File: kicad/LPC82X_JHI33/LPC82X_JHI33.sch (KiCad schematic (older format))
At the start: 20 parts, among them U1 LPC824M201JHI33

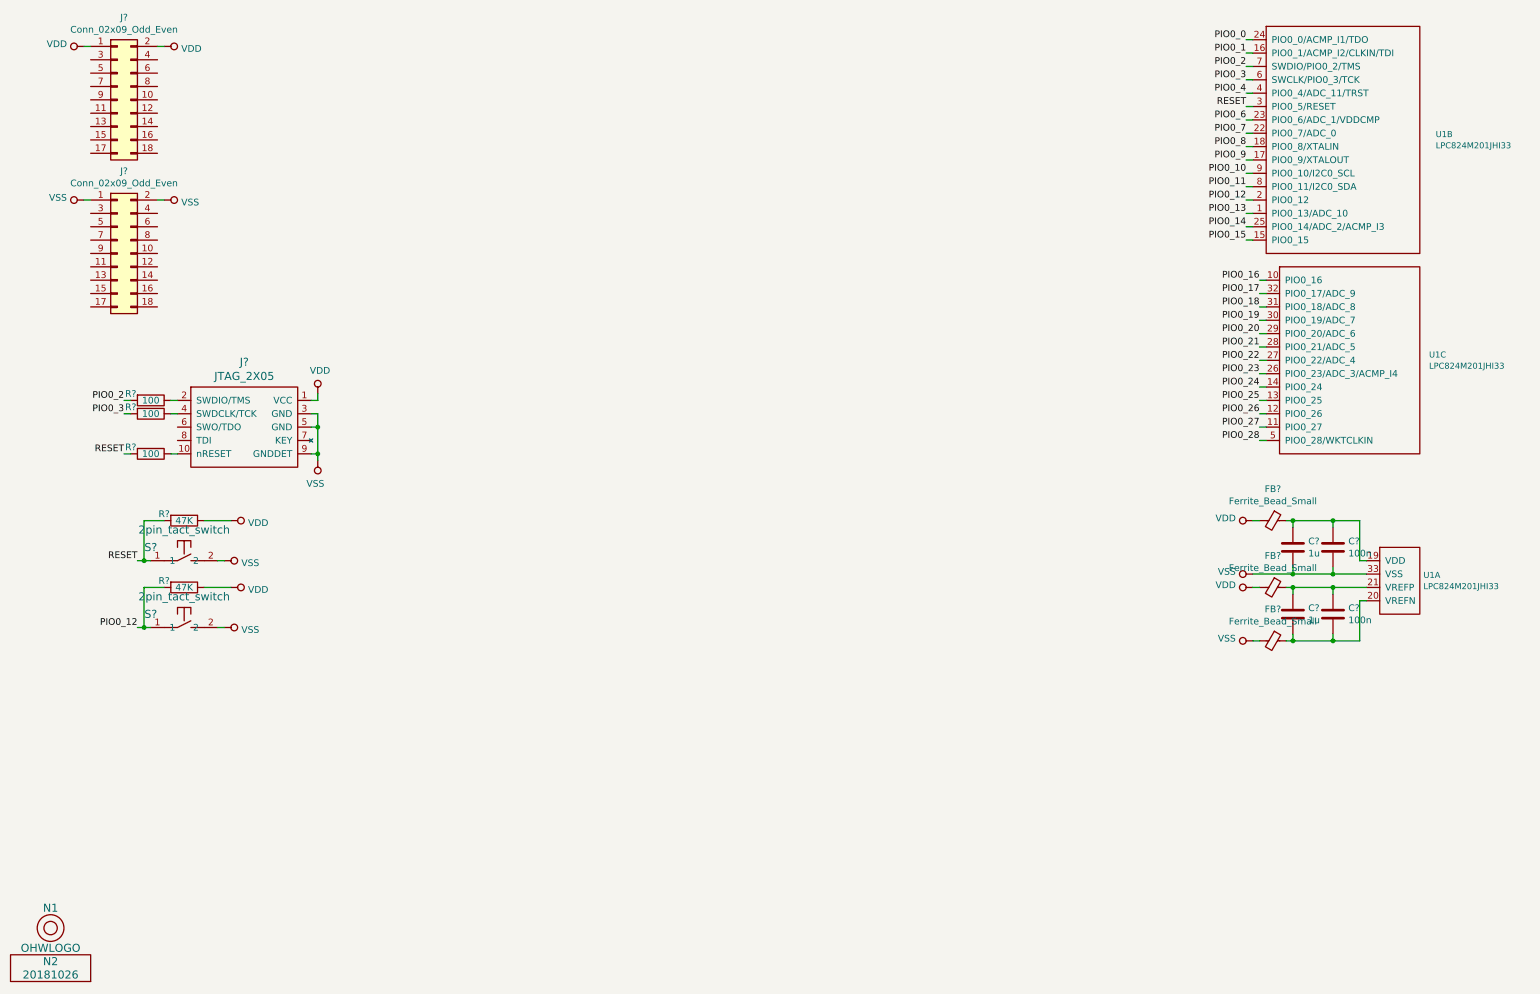
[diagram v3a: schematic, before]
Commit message: updated with solder jumper schematic symbols added some jumpers to the QFN33 breakout
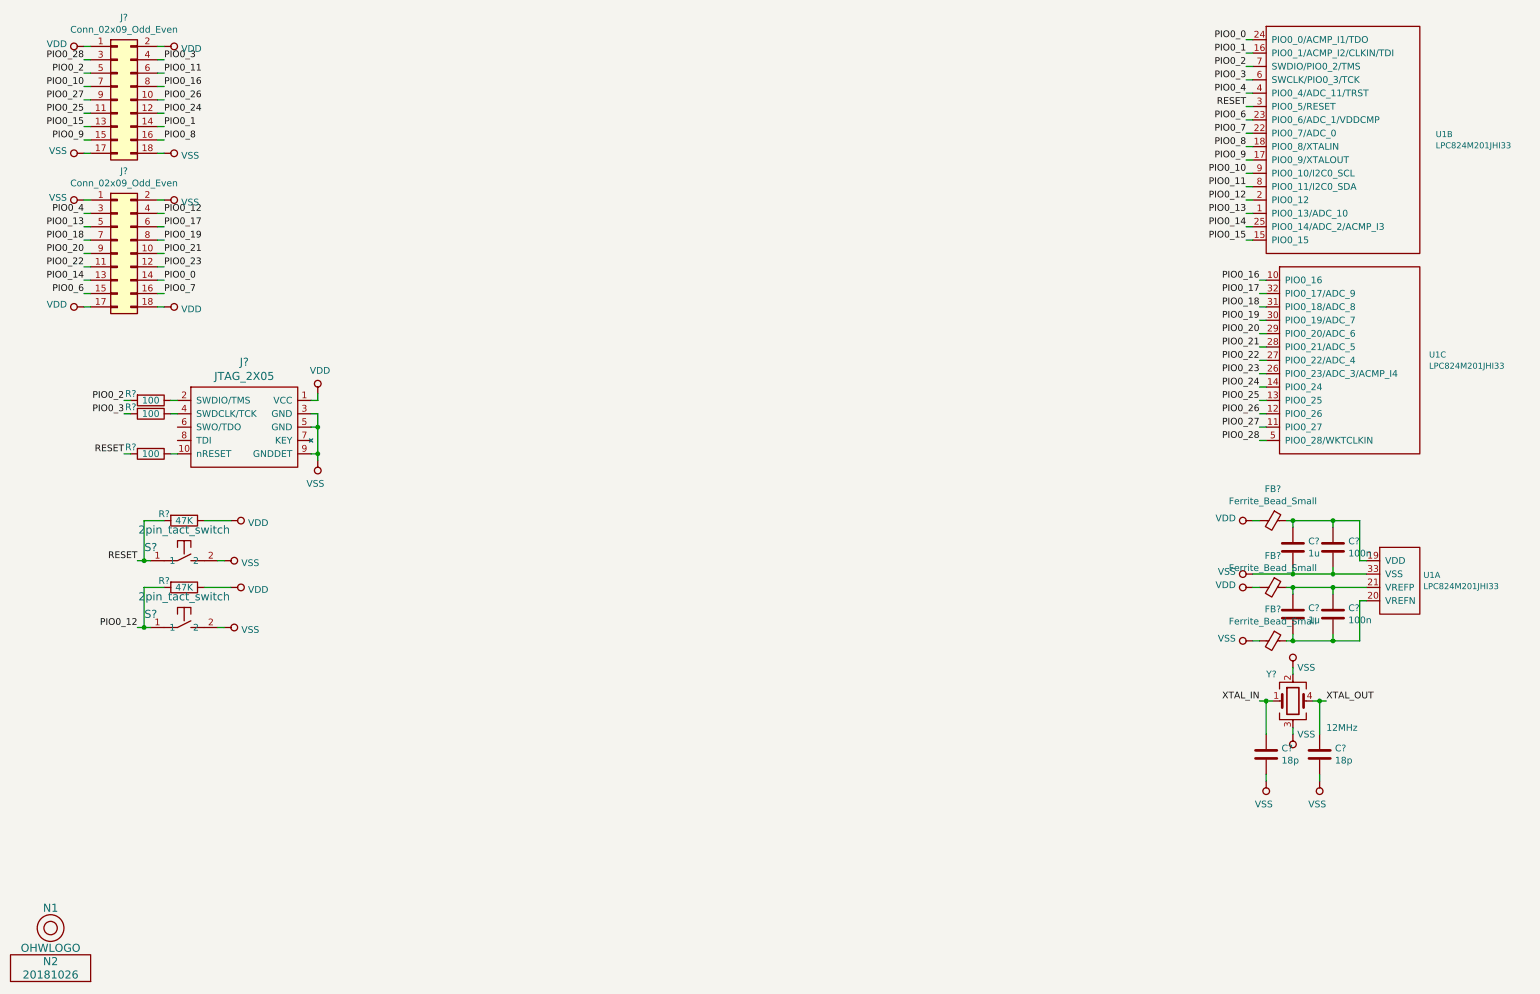
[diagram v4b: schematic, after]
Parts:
- added C? (x2): 18p, SquantorRcl:C_0402, symbol Device:C
- added Y?: 12MHz, symbol Device:Crystal_GND23
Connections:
- net PIO0_0: now also J?.14 (Pin_14)
- net PIO0_1: now also J?.14 (Pin_14)
- net PIO0_10: now also J?.7 (Pin_7)
- net PIO0_11: now also J?.6 (Pin_6)
- net PIO0_12: now also J?.4 (Pin_4)
- net PIO0_13: now also J?.5 (Pin_5)
- net PIO0_14: now also J?.13 (Pin_13)
- net PIO0_15: now also J?.13 (Pin_13)
- net PIO0_16: now also J?.8 (Pin_8)
- net PIO0_17: now also J?.6 (Pin_6)
- net PIO0_18: now also J?.7 (Pin_7)
- net PIO0_19: now also J?.8 (Pin_8)
- net PIO0_2: now also J?.5 (Pin_5)
- net PIO0_20: now also J?.9 (Pin_9)
- net PIO0_21: now also J?.10 (Pin_10)
- net PIO0_22: now also J?.11 (Pin_11)
- net PIO0_23: now also J?.12 (Pin_12)
- net PIO0_24: now also J?.12 (Pin_12)
- net PIO0_25: now also J?.11 (Pin_11)
- net PIO0_26: now also J?.10 (Pin_10)
- net PIO0_27: now also J?.9 (Pin_9)
- net PIO0_28: now also J?.3 (Pin_3)
- net PIO0_3: now also J?.4 (Pin_4)
- net PIO0_4: now also J?.3 (Pin_3)
- net PIO0_6: now also J?.15 (Pin_15)
- net PIO0_7: now also J?.16 (Pin_16)
- net PIO0_8: now also J?.16 (Pin_16)
- net PIO0_9: now also J?.15 (Pin_15)
- net VDD: now also J?.17 (Pin_17), J?.18 (Pin_18)
- net VSS: now also J?.17 (Pin_17), J?.18 (Pin_18), C?.2, C?.2, Y?.2, Y?.3
- new net XTAL_IN: C?.1, Y?.1
- new net XTAL_OUT: C?.1, Y?.4

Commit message: added cystal
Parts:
- added SJ? (x2): SolderJumper_3way_1conn, symbol SquantorSpecial:SolderJumper_3way_1conn
- Y?: footprint (none) -> SquantorCrystal:Crystal_3225_4
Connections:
- net PIO0_8: now also SJ?.1; no longer U1.18 (PIO0_8/XTALIN)
- net PIO0_9: now also SJ?.1; no longer U1.17 (PIO0_9/XTALOUT)
- net XTAL_IN renamed XTALIN
- net XTALIN: now also SJ?.3
- net XTAL_OUT renamed XTALOUT
- net XTALOUT: now also SJ?.3
- new net PIO0_8-XTALIN: SJ?.2, U1.18 (PIO0_8/XTALIN)
- new net PIO0_9-XTALOUT: SJ?.2, U1.17 (PIO0_9/XTALOUT)
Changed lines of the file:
@@
 PIO0_7
 Text Label 9800 1500 2    50   ~ 0
-PIO0_8
+PIO0_8-XTALIN
 Text Label 9800 1600 2    50   ~ 0
-PIO0_9
+PIO0_9-XTALOUT
 Text Label 9800 1700 2    50   ~ 0
 PIO0_10
@@
 F 0 "Y?" H 9950 5850 50  0000 L CNN
 F 1 "12MHz" H 10400 5450 50  0000 L CNN
-F 2 "" H 10150 5650 50  0001 C CNN
+F 2 "SquantorCrystal:Crystal_3225_4" H 10150 5650 50  0001 C CNN
 F 3 "~" H 10150 5650 50  0001 C CNN
 	1    10150 5650
@@
 	10150 5900 10150 5850
 Text Label 9900 5650 2    50   ~ 0
-XTAL_IN
+XTALIN
 Text Label 10400 5650 0    50   ~ 0
-XTAL_OUT
+XTALOUT
+$Comp
+L SquantorSpecial:SolderJumper_3way_1conn SJ?
+U 1 1 5BE59C36
+P 8900 6200
+F 0 "SJ?" H 9000 6350 50  0000 C CNN
+F 1 "SolderJumper_3way_1conn" H 8900 6100 50  0000 C CNN
+F 2 "" H 8900 6200 50  0001 C CNN
+F 3 "" H 8900 6200 50  0001 C CNN
+	1    8900 6200
+	1    0    0    -1
+$EndComp
+$Comp
+L SquantorSpecial:SolderJumper_3way_1conn SJ?
+U 1 1 5BE59D00
+P 7700 6200
+F 0 "SJ?" H 7850 6350 50  0000 R CNN
+F 1 "SolderJumper_3way_1conn" H 8250 6100 50  0000 R CNN
+F 2 "" H 7700 6200 50  0001 C CNN
+F 3 "" H 7700 6200 50  0001 C CNN
+	1    7700 6200
+	1    0    0    -1
+$EndComp
+Text Label 8000 6200 0    50   ~ 0
+XTALIN
+Text Label 9200 6200 0    50   ~ 0
+XTALOUT
+Text Label 7700 6000 1    50   ~ 0
+PIO0_8-XTALIN
+Text Label 7400 6200 2    50   ~ 0
+PIO0_8
+Text Label 8900 6000 1    50   ~ 0
+PIO0_9-XTALOUT
+Text Label 8600 6200 2    50   ~ 0
+PIO0_9
+Wire Wire Line
+	7950 6200 8000 6200
+Wire Wire Line
+	7700 6050 7700 6000
+Wire Wire Line
+	7450 6200 7400 6200
+Wire Wire Line
+	8650 6200 8600 6200
+Wire Wire Line
+	8900 6050 8900 6000
+Wire Wire Line
+	9150 6200 9200 6200
 $EndSCHEMATC

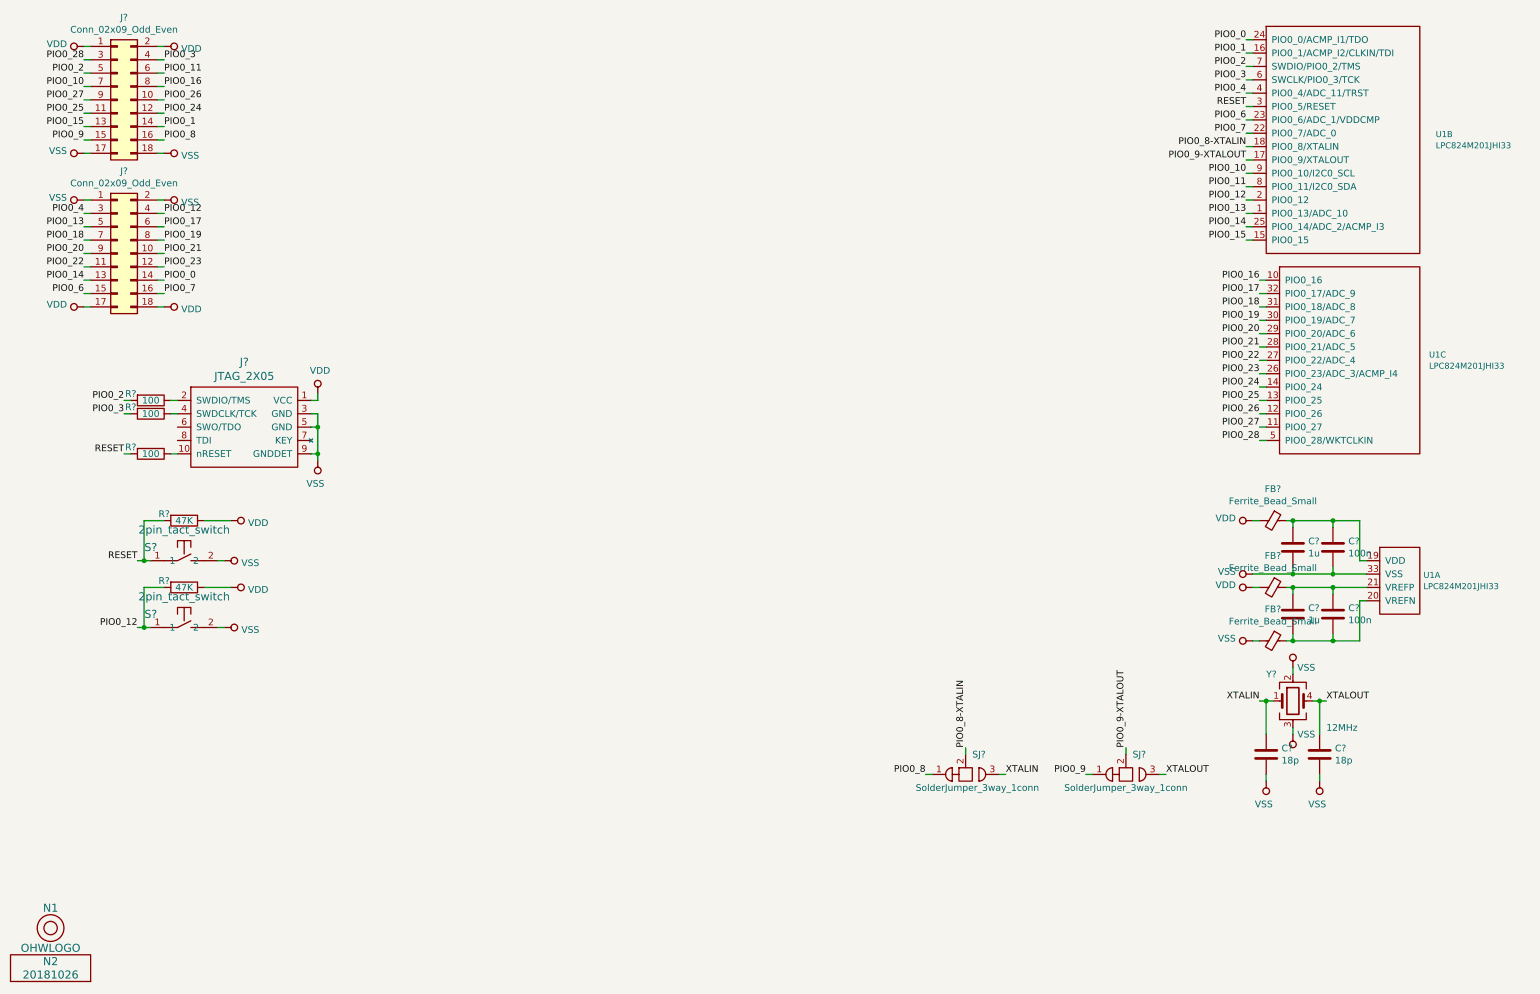
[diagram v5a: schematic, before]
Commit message: finished schematic updated new footprints from submodule
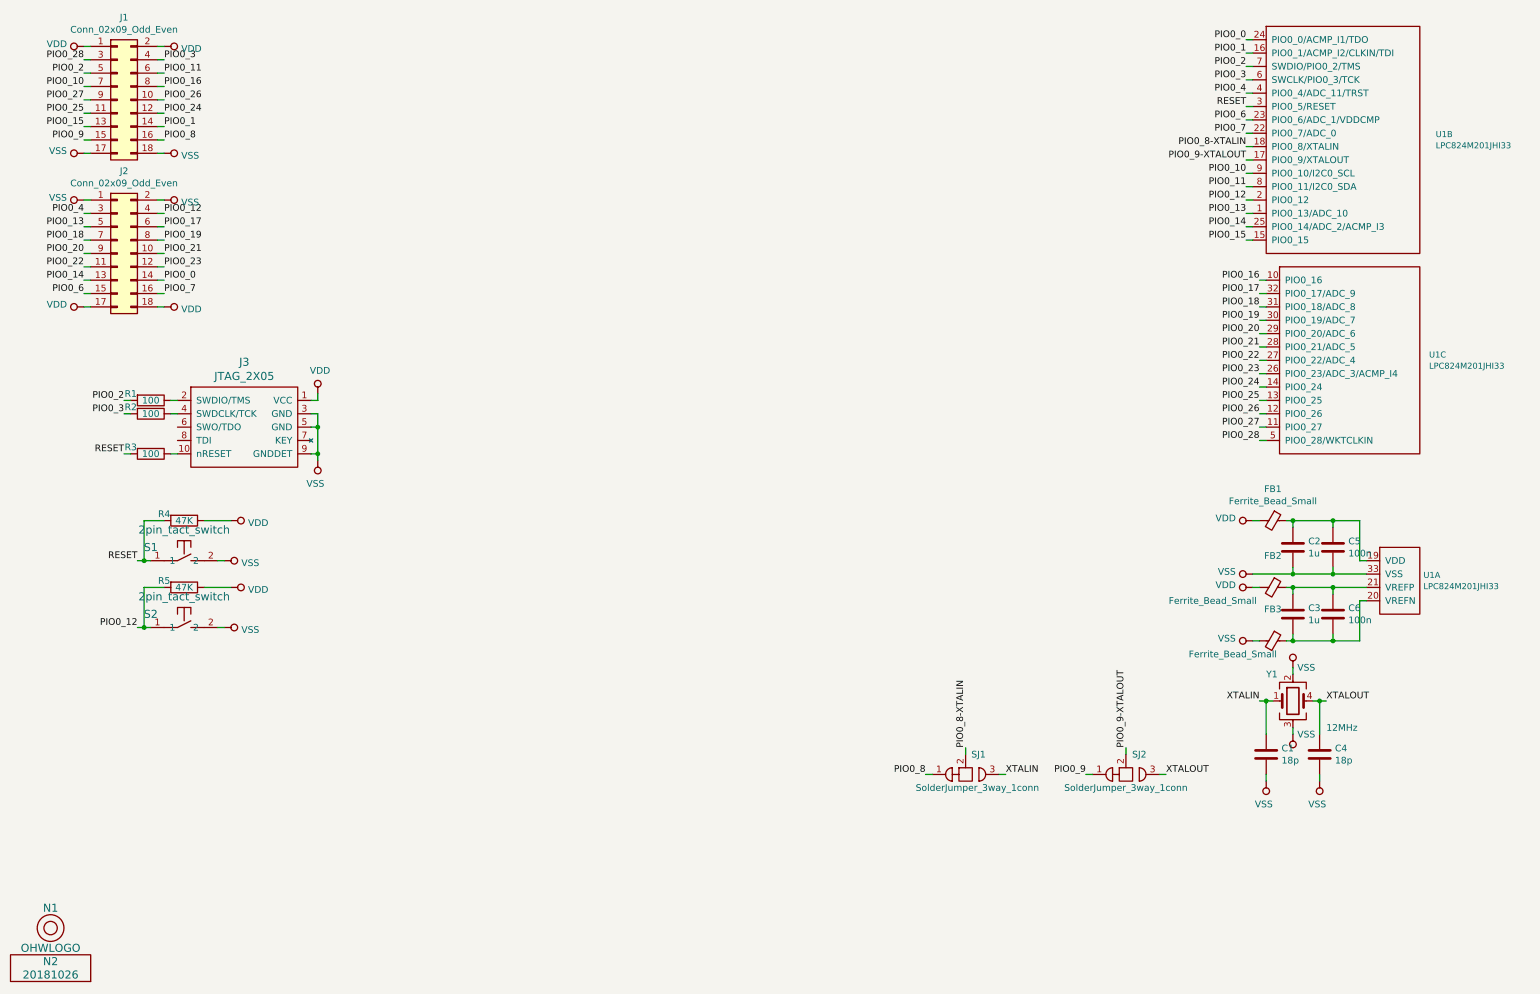
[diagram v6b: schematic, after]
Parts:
- J3: renamed from J?; footprint (none) -> SquantorConnectors:Header-0127-2X05-H006
- SJ1, SJ2: renamed from SJ?; footprint (none) -> SquantorSpecial:solder_jumper_3way_12conn
- gave numbers to parts that had none: 19

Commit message: further pcb placement
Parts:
- added R6, R7: 100k, SquantorRcl:R_0402_hand, symbol Device:R
- C2, C3: footprint SquantorRcl:C_0805 -> SquantorRcl:C_0603
- FB1, FB2, FB3: value Ferrite_Bead_Small -> FB
- Y1: symbol Device:Crystal_GND23 -> Device:Crystal_GND24
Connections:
- net PIO0_2: now also R6.2
- net PIO0_3: now also R7.2
- net VDD: now also R6.1
- net VSS: now also Y1.4, R7.1; no longer Y1.3
- net XTALOUT: now also Y1.3; no longer Y1.4
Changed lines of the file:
@@
 F 0 "C3" H 10265 5046 50  0000 L CNN
 F 1 "1u" H 10265 4955 50  0000 L CNN
-F 2 "SquantorRcl:C_0805" H 10188 4850 50  0001 C CNN
+F 2 "SquantorRcl:C_0603" H 10188 4850 50  0001 C CNN
 F 3 "~" H 10150 5000 50  0001 C CNN
 	1    10150 5000
@@
 P 10000 4800
 F 0 "FB2" V 9763 4800 50  0000 C CNN
-F 1 "Ferrite_Bead_Small" V 10100 4350 50  0000 C CNN
+F 1 "FB" V 10100 4350 50  0000 C CNN
 F 2 "SquantorRcl:C_0402" V 9930 4800 50  0001 C CNN
 F 3 "~" H 10000 4800 50  0001 C CNN
@@
 P 10000 5200
 F 0 "FB3" V 9763 5200 50  0000 C CNN
-F 1 "Ferrite_Bead_Small" V 10100 4900 50  0000 C CNN
+F 1 "FB" V 10100 4900 50  0000 C CNN
 F 2 "SquantorRcl:C_0402" V 9930 5200 50  0001 C CNN
 F 3 "~" H 10000 5200 50  0001 C CNN
@@
 F 0 "C2" H 10265 4546 50  0000 L CNN
 F 1 "1u" H 10265 4455 50  0000 L CNN
-F 2 "SquantorRcl:C_0805" H 10188 4350 50  0001 C CNN
+F 2 "SquantorRcl:C_0603" H 10188 4350 50  0001 C CNN
 F 3 "~" H 10150 4500 50  0001 C CNN
 	1    10150 4500
@@
 P 10000 4300
 F 0 "FB1" V 9763 4300 50  0000 C CNN
-F 1 "Ferrite_Bead_Small" V 9854 4300 50  0000 C CNN
+F 1 "FB" V 9854 4300 50  0000 C CNN
 F 2 "SquantorRcl:C_0402" V 9930 4300 50  0001 C CNN
 F 3 "~" H 10000 4300 50  0001 C CNN
@@
 	1750 3500 1800 3500
 Wire Wire Line
-	1450 3500 1400 3500
-Wire Wire Line
-	1450 3400 1400 3400
-Text Label 1400 3400 2    50   ~ 0
+	1450 3500 1350 3500
+Wire Wire Line
+	1450 3400 1350 3400
+Text Label 1350 3400 2    50   ~ 0
 PIO0_2
-Text Label 1400 3500 2    50   ~ 0
+Text Label 1350 3500 2    50   ~ 0
 PIO0_3
 $Comp
@@
 	1800 3800 1750 3800
 Wire Wire Line
-	1450 3800 1400 3800
-Text Label 1400 3800 2    50   ~ 0
+	1450 3800 1350 3800
+Text Label 1350 3800 2    50   ~ 0
 RESET
 $Comp
@@
 Wire Wire Line
 	10350 6200 10350 6250
-$Comp
-L Device:Crystal_GND23 Y1
-U 1 1 5BE1D5EF
-P 10150 5650
-F 0 "Y1" H 9950 5850 50  0000 L CNN
-F 1 "12MHz" H 10400 5450 50  0000 L CNN
-F 2 "SquantorCrystal:Crystal_3225_4" H 10150 5650 50  0001 C CNN
-F 3 "~" H 10150 5650 50  0001 C CNN
-	1    10150 5650
-	1    0    0    -1
-$EndComp
 Wire Wire Line
 	10000 5650 9950 5650
@@
 Wire Wire Line
 	9150 6200 9200 6200
+$Comp
+L Device:R R7
+U 1 1 5BECCB56
+P 1600 3150
+F 0 "R7" V 1550 3000 50  0000 C CNN
+F 1 "100k" V 1600 3150 50  0000 C CNN
+F 2 "SquantorRcl:R_0402_hand" V 1530 3150 50  0001 C CNN
+F 3 "~" H 1600 3150 50  0001 C CNN
+	1    1600 3150
+	0    1    1    0
+$EndComp
+$Comp
+L Device:R R6
+U 1 1 5BECCC51
+P 1600 3050
+F 0 "R6" V 1550 2900 50  0000 C CNN
+F 1 "100k" V 1600 3050 50  0000 C CNN
+F 2 "SquantorRcl:R_0402_hand" V 1530 3050 50  0001 C CNN
+F 3 "~" H 1600 3050 50  0001 C CNN
+	1    1600 3050
+	0    1    1    0
+$EndComp
+$Comp
+L power:VSS #PWR0123
+U 1 1 5BECCC9B
+P 1800 3150
+F 0 "#PWR0123" H 1800 3000 50  0001 C CNN
+F 1 "VSS" V 1817 3278 50  0000 L CNN
+F 2 "" H 1800 3150 50  0001 C CNN
+F 3 "" H 1800 3150 50  0001 C CNN
+	1    1800 3150
+	0    1    1    0
+$EndComp
+$Comp
+L power:VDD #PWR0124
+U 1 1 5BECCD37
+P 1800 3050
+F 0 "#PWR0124" H 1800 2900 50  0001 C CNN
+F 1 "VDD" V 1817 3178 50  0000 L CNN
+F 2 "" H 1800 3050 50  0001 C CNN
+F 3 "" H 1800 3050 50  0001 C CNN
+	1    1800 3050
+	0    1    1    0
+$EndComp
+Wire Wire Line
+	1800 3150 1750 3150
+Wire Wire Line
+	1750 3050 1800 3050
+Text Label 1350 3150 2    50   ~ 0
+PIO0_3
+Text Label 1350 3050 2    50   ~ 0
+PIO0_2
+Wire Wire Line
+	1450 3150 1350 3150
+Wire Wire Line
+	1450 3050 1350 3050
+$Comp
+L Device:Crystal_GND24 Y1
+U 1 1 5BE1D5EF
+P 10150 5650
+F 0 "Y1" H 9950 5850 50  0000 L CNN
+F 1 "12MHz" H 10400 5450 50  0000 L CNN
+F 2 "SquantorCrystal:Crystal_3225_4" H 10150 5650 50  0001 C CNN
+F 3 "~" H 10150 5650 50  0001 C CNN
+	1    10150 5650
+	1    0    0    -1
+$EndComp
 $EndSCHEMATC
